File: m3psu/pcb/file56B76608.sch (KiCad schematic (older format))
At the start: 33 parts

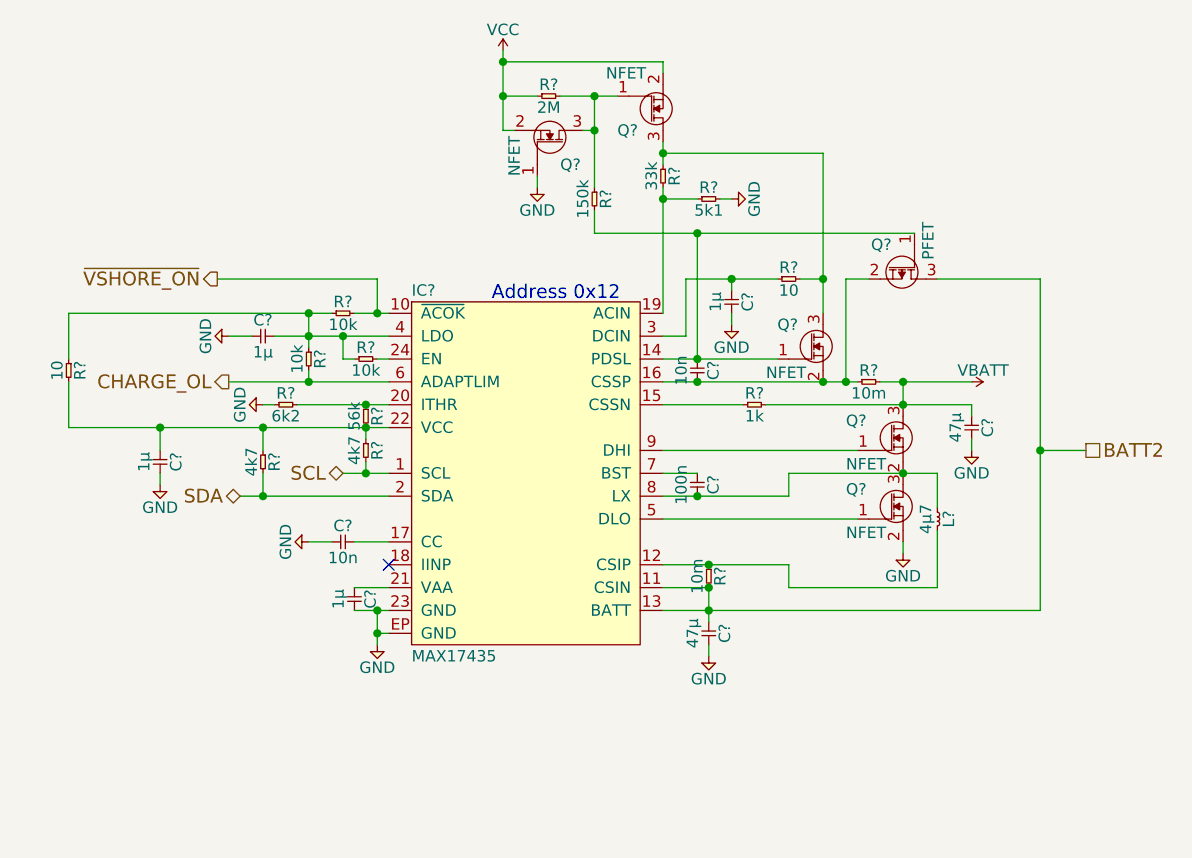
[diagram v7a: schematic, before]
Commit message: Changes to Li-ion charger, north local interconnect.
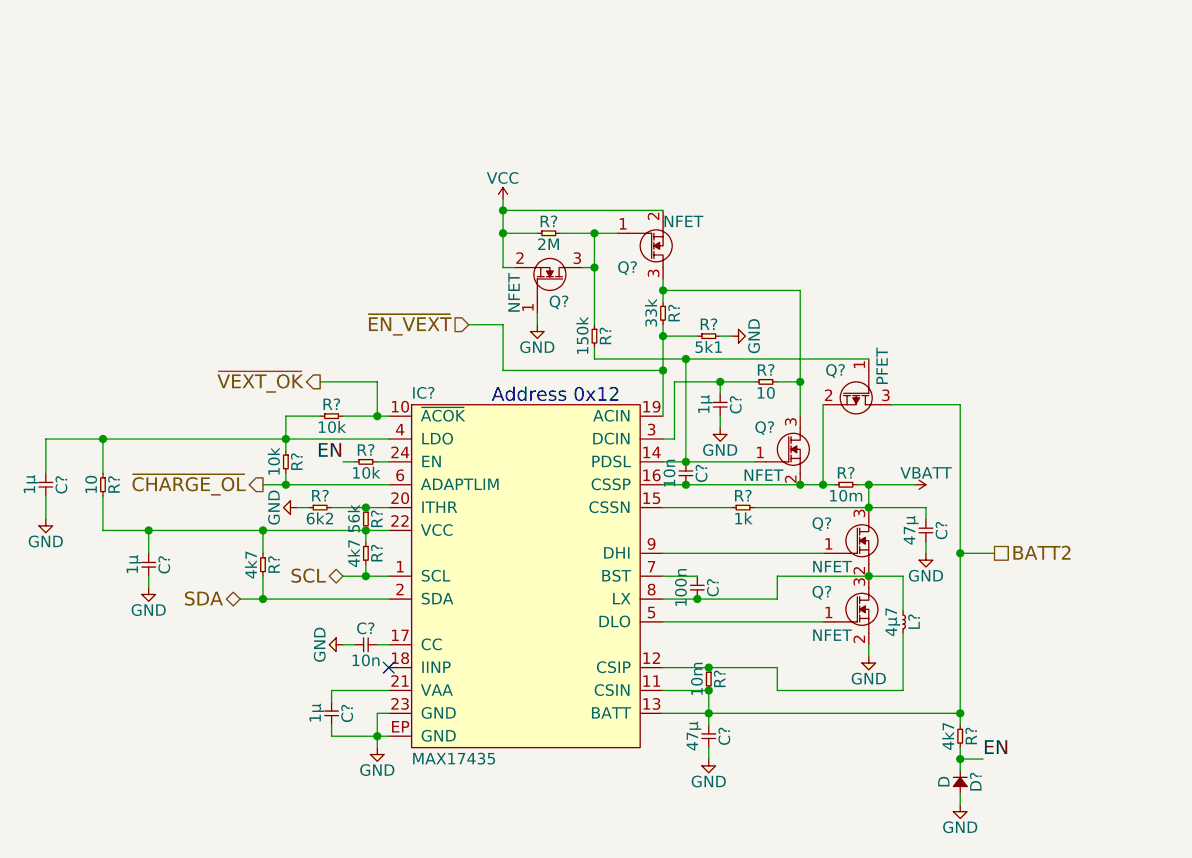
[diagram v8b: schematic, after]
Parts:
- added D?: D, symbol D
- added R?: 4k7, agg:0402, symbol R
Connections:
- net BATT2: now also R?.1
- net GND: now also C?.2, D?.2; no longer C?.1
- net ~EN_VEXT: now reaches IC?.19 (ACIN), R?.1, R?.2
- net at IC?.4 (LDO), R?.1, R?.1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: now also C?.1; no longer C?.2, R?.1
- net CHARGE_OL renamed ~CHARGE_OL
- net ~VSHORE_ON renamed ~VEXT_OK
- new net EN: D?.1, R?.1, R?.2
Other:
- moved on the sheet: C?, IC?, L?, Q?, R?
